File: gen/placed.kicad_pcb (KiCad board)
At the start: 2 copper layers, 100 x 80 mm, 314 parts, among them J101 24VDC IN, J201 SWD, J301 USB-C, J401 HR911105A, J402 RS485, J501 OUT 1-8, J502 OUT 9-16, J701 AI 1-10, J702 mA SELECT, J703 AI PWR/COM, Q301 MMBT3904, Q302 MMBT3904, Q303 MMBT3906, Q501 DMN6075S, Q502 DMN6075S, Q503 DMN6075S, Q504 DMN6075S, Q505 DMN6075S, Q506 DMN6075S, Q507 DMN6075S, Q508 DMN6075S, Q509 DMN6075S, Q510 DMN6075S, Q511 DMN6075S, Q512 DMN6075S, Q513 DMN6075S, Q514 DMN6075S, Q515 DMN6075S, Q516 DMN6075S, SW201 RESET, SW202 BOOT, U101 LMR16006YQ5, U102 AMS1117-3.3, U200 STM32F407VET6, U201 REF3030, U301 USBLC6-2SC6, U302 CH340C, U400 W5500, U401 SP3485EN, U501 TLP291-4, U502 TLP291-4, U503 TLP291-4, U504 TLP291-4, Y201 8MHz 20pF, Y401 25MHz 18pF

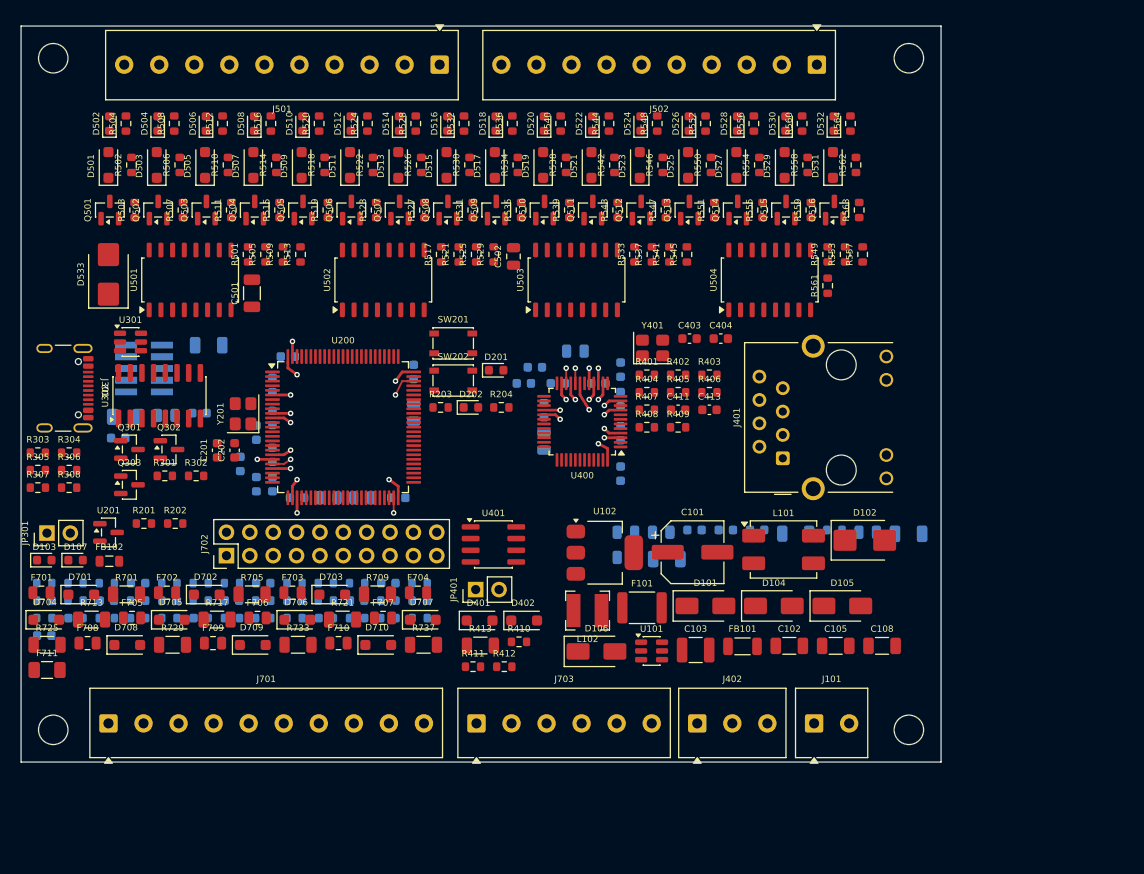
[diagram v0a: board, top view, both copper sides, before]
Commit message: - bỏ các mạch 0-10v, RS485 RTU
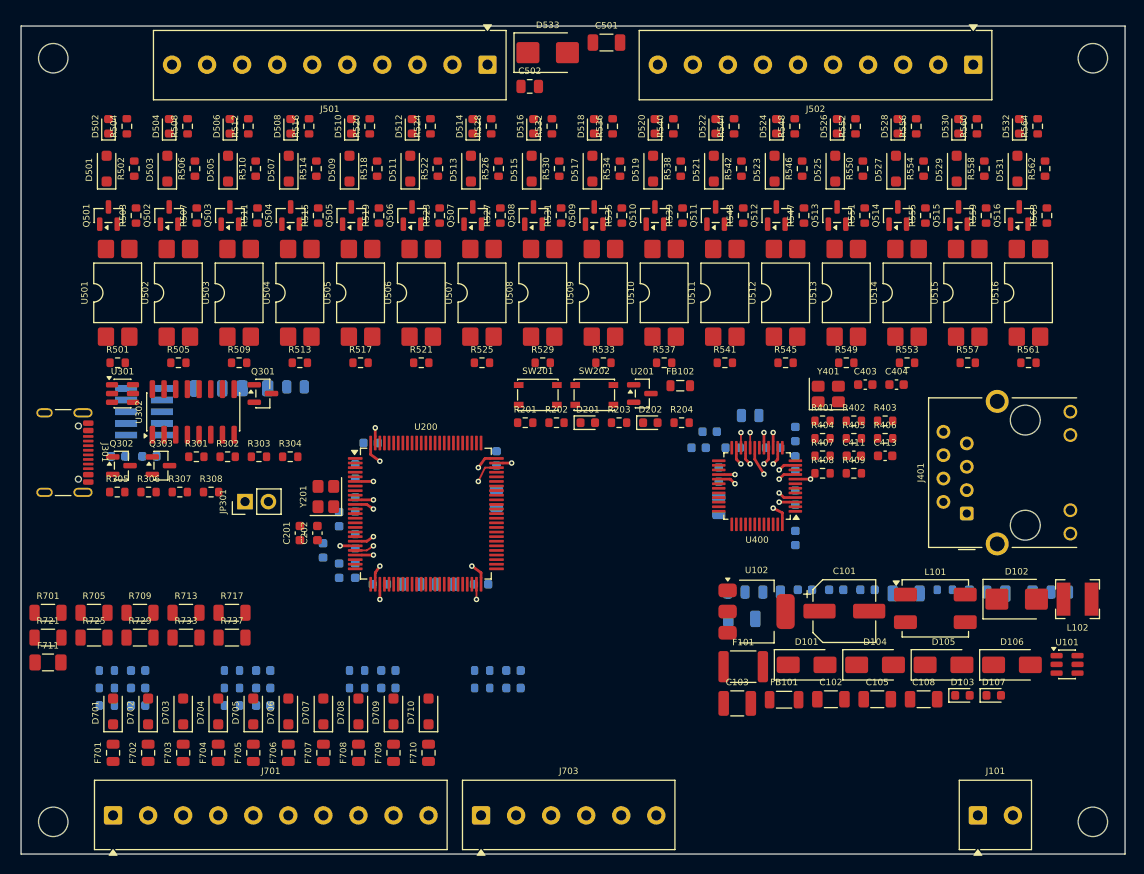
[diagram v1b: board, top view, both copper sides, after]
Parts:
- removed D401, D402: SMF12CA, Diode_SMD:D_SOD-123F
- removed J402: RS485, TerminalBlock_Phoenix:TerminalBlock_Phoenix_MKDS-1-3-3.81_1x03_P3.81mm_Horizontal
- removed J702: mA SELECT, Connector_PinHeader_2.54mm:PinHeader_2x10_P2.54mm_Vertical
- removed JP401: TERM 120R, Connector_PinHeader_2.54mm:PinHeader_1x02_P2.54mm_Vertical
- removed R410: 10k, Resistor_SMD:R_0603_1608Metric
- removed R411, R412: 680, Resistor_SMD:R_0603_1608Metric
- removed R413: 120, Resistor_SMD:R_1206_3216Metric
- removed R702, R706, R710, R714, R718, R722, R726, R730, R734, R738: 47k 0.1%, Resistor_SMD:R_0603_1608Metric
- removed R703, R707, R711, R715, R719, R723, R727, R731, R735, R739: 18k 0.1%, Resistor_SMD:R_0603_1608Metric
- removed U401: SP3485EN, Package_SO:SOIC-8_3.9x4.9mm_P1.27mm
- added U505: PC817 (SMD), Package_DIP:SMDIP-4_W9.53mm, F.Cu at (86.9, 79.0)
- added U506: PC817 (SMD), Package_DIP:SMDIP-4_W9.53mm, F.Cu at (93.5, 79.0)
- added U507: PC817 (SMD), Package_DIP:SMDIP-4_W9.53mm, F.Cu at (100.1, 79.0)
- added U508: PC817 (SMD), Package_DIP:SMDIP-4_W9.53mm, F.Cu at (106.7, 79.0)
- added U509: PC817 (SMD), Package_DIP:SMDIP-4_W9.53mm, F.Cu at (113.3, 79.0)
- added U510: PC817 (SMD), Package_DIP:SMDIP-4_W9.53mm, F.Cu at (119.9, 79.0)
- added U511: PC817 (SMD), Package_DIP:SMDIP-4_W9.53mm, F.Cu at (126.5, 79.0)
- added U512: PC817 (SMD), Package_DIP:SMDIP-4_W9.53mm, F.Cu at (133.1, 79.0)
- added U513: PC817 (SMD), Package_DIP:SMDIP-4_W9.53mm, F.Cu at (139.7, 79.0)
- added U514: PC817 (SMD), Package_DIP:SMDIP-4_W9.53mm, F.Cu at (146.3, 79.0)
- added U515: PC817 (SMD), Package_DIP:SMDIP-4_W9.53mm, F.Cu at (152.9, 79.0)
- added U516: PC817 (SMD), Package_DIP:SMDIP-4_W9.53mm, F.Cu at (159.5, 79.0)
- D701, D702, D703, D704, D705, D706, D707, D708, D709, D710: value SMF12CA -> SMF5.0CA
- J701: value AI 1-10 -> AI 1-10 (4-20mA)
- R701, R705, R709, R713, R717, R721, R725, R729, R733, R737: value 499 0.1% 0.25W -> 120 0.1% 25ppm
- R704, R708, R712, R716, R720, R724, R728, R732, R736, R740: value 1k -> 4.7k
- U501, U502, U503, U504: value TLP291-4 -> PC817 (SMD); footprint Package_SO:SOIC-16_4.55x10.3mm_P1.27mm -> Package_DIP:SMDIP-4_W9.53mm
- moved D107 100.9 mm to (155.7, 122.8)
- moved D103 100.9 mm to (152.3, 122.8)
- moved FB102 64.9 mm to (121.7, 89.1)
- moved U201 60.0 mm to (117.5, 89.9)
- moved D533 53.5 mm to (107.2, 52.9), turned to 0 degrees
- moved L102 53.3 mm to (164.8, 112.3)
- moved U504 51.1 mm to (80.3, 79.0)
- moved C113 47.3 mm to (162.9, 111.5)
- moved C501 47.2 mm to (113.6, 51.8), turned to 0 degrees
- moved U101 45.2 mm to (163.7, 119.4)
- moved D106 45.2 mm to (157.7, 119.4)
- moved C704 44.8 mm to (103.5, 120.1)
- moved R716 44.8 mm to (100.1, 120.1)
- moved R202 42.9 mm to (108.2, 93.1)
- moved R201 42.9 mm to (104.8, 93.1)
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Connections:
- net /Ethernet + RS485/ETH_1V2 renamed /Ethernet/ETH_1V2
- net /Ethernet + RS485/ETH_ACT_LED renamed /Ethernet/ETH_ACT_LED
- net /Ethernet + RS485/ETH_EXRES renamed /Ethernet/ETH_EXRES
- net /Ethernet + RS485/ETH_LEDG_A renamed /Ethernet/ETH_LEDG_A
- net /Ethernet + RS485/ETH_LEDY_A renamed /Ethernet/ETH_LEDY_A
- net /Ethernet + RS485/ETH_LINK_LED renamed /Ethernet/ETH_LINK_LED
- net /Ethernet + RS485/ETH_RCT renamed /Ethernet/ETH_RCT
- net /Ethernet + RS485/ETH_RXMID renamed /Ethernet/ETH_RXMID
- net /Ethernet + RS485/ETH_RXN renamed /Ethernet/ETH_RXN
- net /Ethernet + RS485/ETH_RXP renamed /Ethernet/ETH_RXP
- net /Ethernet + RS485/ETH_TOCAP renamed /Ethernet/ETH_TOCAP
- net /Ethernet + RS485/ETH_TXN renamed /Ethernet/ETH_TXN
- net /Ethernet + RS485/ETH_TXP renamed /Ethernet/ETH_TXP
- net /Ethernet + RS485/ETH_XI renamed /Ethernet/ETH_XI
- net /Ethernet + RS485/ETH_XO renamed /Ethernet/ETH_XO
- R701 pad 1: /10 ngo vao analog/AI1_SH -> /10 ngo vao analog/AI1_IN
- R704 pad 1: Net-(R702-Pad2) -> /10 ngo vao analog/AI1_IN
- R705 pad 1: /10 ngo vao analog/AI2_SH -> /10 ngo vao analog/AI2_IN
- R708 pad 1: Net-(R706-Pad2) -> /10 ngo vao analog/AI2_IN
- R709 pad 1: /10 ngo vao analog/AI3_SH -> /10 ngo vao analog/AI3_IN
- R712 pad 1: Net-(R710-Pad2) -> /10 ngo vao analog/AI3_IN
- R713 pad 1: /10 ngo vao analog/AI4_SH -> /10 ngo vao analog/AI4_IN
- R716 pad 1: Net-(R714-Pad2) -> /10 ngo vao analog/AI4_IN
- R717 pad 1: /10 ngo vao analog/AI5_SH -> /10 ngo vao analog/AI5_IN
- R720 pad 1: Net-(R718-Pad2) -> /10 ngo vao analog/AI5_IN
- R721 pad 1: /10 ngo vao analog/AI6_SH -> /10 ngo vao analog/AI6_IN
- R724 pad 1: Net-(R722-Pad2) -> /10 ngo vao analog/AI6_IN
- R725 pad 1: /10 ngo vao analog/AI7_SH -> /10 ngo vao analog/AI7_IN
- R728 pad 1: Net-(R726-Pad2) -> /10 ngo vao analog/AI7_IN
- R729 pad 1: /10 ngo vao analog/AI8_SH -> /10 ngo vao analog/AI8_IN
- R732 pad 1: Net-(R730-Pad2) -> /10 ngo vao analog/AI8_IN
- R733 pad 1: /10 ngo vao analog/AI9_SH -> /10 ngo vao analog/AI9_IN
- R736 pad 1: Net-(R734-Pad2) -> /10 ngo vao analog/AI9_IN
- R737 pad 1: /10 ngo vao analog/AI10_SH -> /10 ngo vao analog/AI10_IN
- R740 pad 1: Net-(R738-Pad2) -> /10 ngo vao analog/AI10_IN
- U200 pad 46: RS485_DE -> unconnected-(U200-PE15-Pad46)
- U200 pad 47: RS485_TX -> unconnected-(U200-PB10-Pad47)
- U200 pad 48: RS485_RX -> unconnected-(U200-PB11-Pad48)
- U501 pad 3: Net-(R505-Pad2) -> Net-(Q501-G)
- U501 pad 4: GND -> Net-(R502-Pad2)
- U502 pad 1: Net-(R517-Pad2) -> Net-(R505-Pad2)
- U502 pad 3: Net-(R521-Pad2) -> Net-(Q502-G)
- U502 pad 4: GND -> Net-(R506-Pad2)
- U503 pad 1: Net-(R533-Pad2) -> Net-(R509-Pad2)
- U503 pad 3: Net-(R537-Pad2) -> Net-(Q503-G)
- U503 pad 4: GND -> Net-(R510-Pad2)
- U504 pad 1: Net-(R549-Pad2) -> Net-(R513-Pad2)
- U504 pad 3: Net-(R553-Pad2) -> Net-(Q504-G)
- U504 pad 4: GND -> Net-(R514-Pad2)
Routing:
- net +3V3: track 17.2 -> 18.2 mm, vias 13 -> 14
- net GND: track 16.1 -> 17.1 mm, vias 12 -> 13
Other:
- board size 100 x 80 mm -> 120 x 90 mm
- board text added: "PLC STM32F407 MODBUS TCP - 16DO/10AI v1.1"
- board text removed: "PLC STM32F407 MODBUS TCP - 16DO/10AI v1.0"

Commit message: - bỏ các cầu chì thêm mô tả cho từng linh kiên
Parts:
- removed F701, F702, F703, F704, F705, F706, F707, F708, F709, F710: 50mA, Fuse:Fuse_0805_2012Metric
- F711: value 200mA -> MF-MSMF050-2 0.5A/60V; footprint Fuse:Fuse_1206_3216Metric -> Fuse:Fuse_1812_4532Metric
- moved F711 49.7 mm to (102.5, 116.0)
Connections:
- J701 pad 1: /10 ngo vao analog/AI1_T -> /10 ngo vao analog/AI1_IN
- J701 pad 10: /10 ngo vao analog/AI10_T -> /10 ngo vao analog/AI10_IN
- J701 pad 2: /10 ngo vao analog/AI2_T -> /10 ngo vao analog/AI2_IN
- J701 pad 3: /10 ngo vao analog/AI3_T -> /10 ngo vao analog/AI3_IN
- J701 pad 4: /10 ngo vao analog/AI4_T -> /10 ngo vao analog/AI4_IN
- J701 pad 5: /10 ngo vao analog/AI5_T -> /10 ngo vao analog/AI5_IN
- J701 pad 6: /10 ngo vao analog/AI6_T -> /10 ngo vao analog/AI6_IN
- J701 pad 7: /10 ngo vao analog/AI7_T -> /10 ngo vao analog/AI7_IN
- J701 pad 8: /10 ngo vao analog/AI8_T -> /10 ngo vao analog/AI8_IN
- J701 pad 9: /10 ngo vao analog/AI9_T -> /10 ngo vao analog/AI9_IN

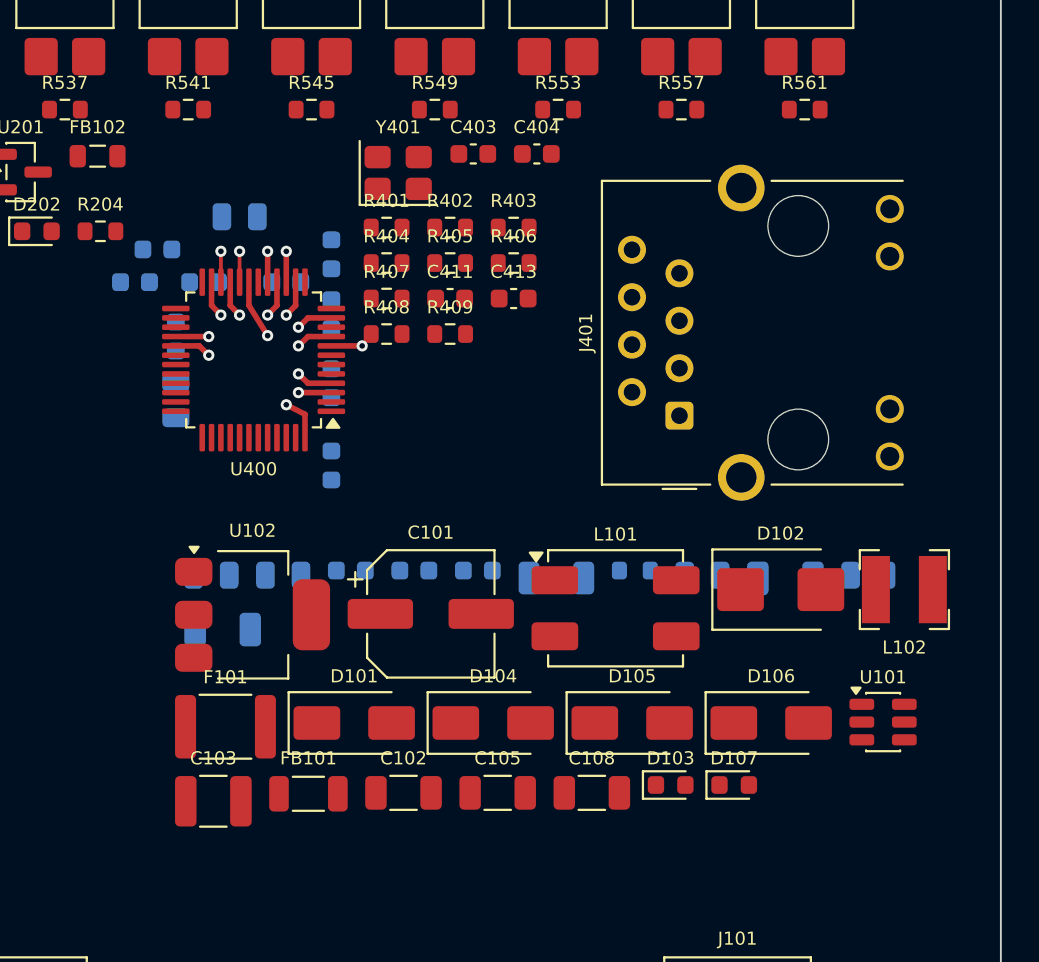
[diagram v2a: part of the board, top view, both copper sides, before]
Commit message: - thay w5500 bằng module w5500 lite
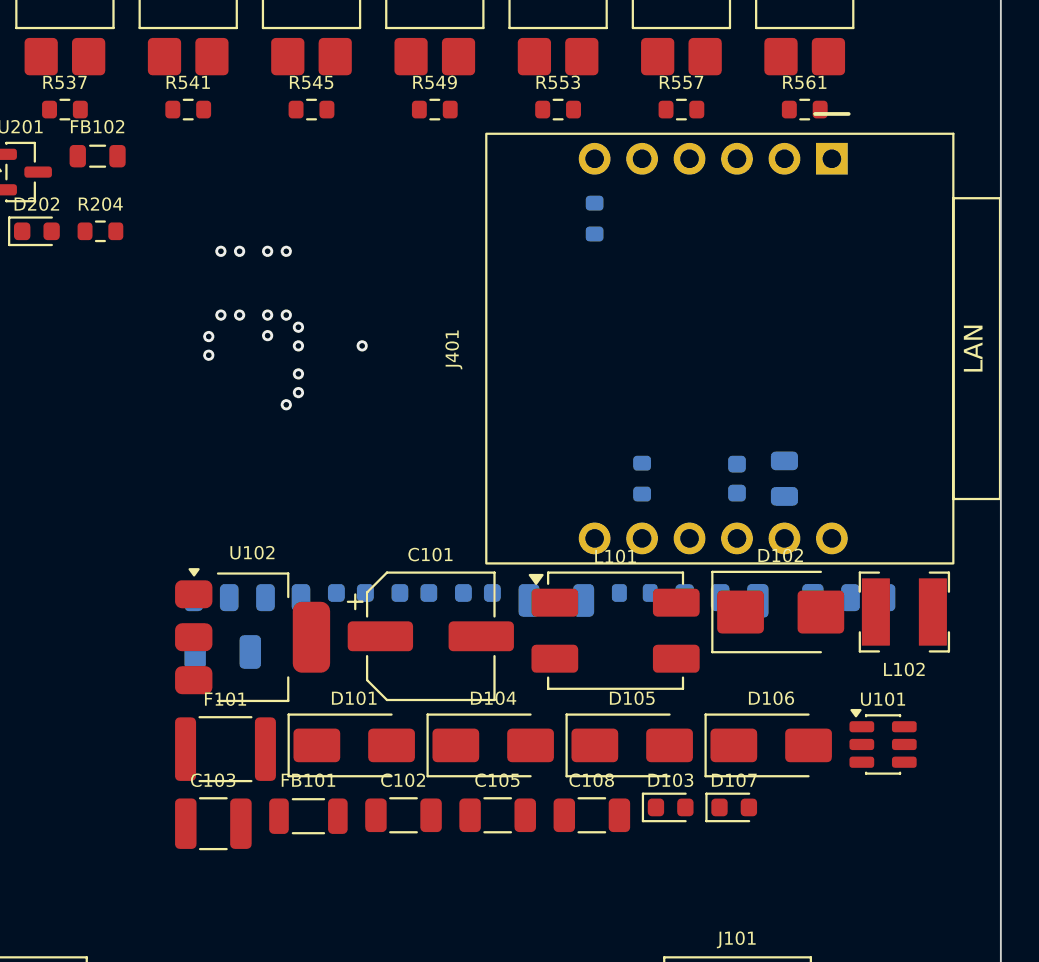
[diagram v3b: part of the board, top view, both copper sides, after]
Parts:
- removed C403, C404: 18pF, Capacitor_SMD:C_0603_1608Metric
- removed C405, C406, C407, C408, C409, C414, C415: 100nF, Capacitor_SMD:C_0603_1608Metric
- removed C410: 10uF, Capacitor_SMD:C_0805_2012Metric
- removed C411: 6.8nF, Capacitor_SMD:C_0603_1608Metric
- removed C412, C413: 10nF, Capacitor_SMD:C_0603_1608Metric
- removed R403: 10k, Resistor_SMD:R_0603_1608Metric
- removed R404, R405, R406, R407: 49.9 1%, Resistor_SMD:R_0603_1608Metric
- removed R408, R409: 330, Resistor_SMD:R_0603_1608Metric
- removed U400: W5500, Package_QFP:LQFP-48_7x7mm_P0.5mm
- removed Y401: 25MHz 18pF, Crystal:Crystal_SMD_3225-4Pin_3.2x2.5mm
- C401: value 4.7uF -> 10uF
- C402: value 10nF -> 100nF
- J401: value HR911105A -> W5500 Lite module; footprint Connector_RJ:RJ45_Hanrun_HR911105A_Horizontal -> PLC:W5500_Lite_Module
- R401: value 12.4k 1% -> 10k; moved to B.Cu
- R402: moved to B.Cu
- moved C402 33.4 mm to (155.9, 106.4), turned to 90 degrees
- moved C401 32.4 mm to (158.4, 106.4), turned to 90 degrees
- moved R402 16.9 mm to (150.8, 106.4), turned to 90 degrees
- moved J401 16.0 mm to (161.0, 89.2), turned to -90 degrees
- moved R401 11.1 mm to (148.3, 92.4), turned to 90 degrees
- moved C101 1.20 mm to (139.5, 114.8)
- moved C102 1.20 mm to (138.0, 124.4)
- moved C103 1.20 mm to (127.8, 124.8)
- moved C105 1.20 mm to (143.1, 124.4)
- moved C108 1.20 mm to (148.1, 124.4)
- moved C109 1.20 mm to (128.3, 115.6)
- moved C111 1.20 mm to (158.5, 112.9)
- moved D101 1.20 mm to (135.4, 120.6)
- moved D102 1.20 mm to (158.2, 113.5)
- moved D103 1.20 mm to (152.3, 124.0)
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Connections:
- C401 pad 1: /Ethernet/ETH_TOCAP -> +3V3
- C402 pad 1: /Ethernet/ETH_1V2 -> +3V3
- J401 pad 1: /Ethernet/ETH_TXP -> GND
- J401 pad 10: /Ethernet/ETH_LINK_LED -> unconnected-(J401-NC-Pad10)
- J401 pad 11: /Ethernet/ETH_ACT_LED -> ETH_RST
- J401 pad 12: /Ethernet/ETH_LEDY_A -> ETH_MISO
- J401 pad 2: /Ethernet/ETH_TXN -> GND
- J401 pad 3: /Ethernet/ETH_RXP -> ETH_MOSI
- J401 pad 4: +3V3 -> ETH_SCK
- J401 pad 5: /Ethernet/ETH_RCT -> ETH_CS
- J401 pad 6: /Ethernet/ETH_RXN -> ETH_INT
- J401 pad 7: unconnected-(J401-NC-Pad7) -> GND
- J401 pad 8: GND -> +3V3
- J401 pad 9: /Ethernet/ETH_LEDG_A -> +3V3
- R401 pad 1: /Ethernet/ETH_EXRES -> +3V3
- R401 pad 2: GND -> ETH_INT
- R402 pad 2: ETH_INT -> ETH_RST
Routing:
- net GND: track 17.1 -> 5.56 mm
- net +3V3: track 18.2 -> 10.4 mm, vias 14 -> 16
- net /Ethernet/ETH_TOCAP: track 0.95 -> 0.00 mm, vias 1 -> 0
- net /Ethernet/ETH_1V2: track 0.95 -> 0.00 mm, vias 1 -> 0
